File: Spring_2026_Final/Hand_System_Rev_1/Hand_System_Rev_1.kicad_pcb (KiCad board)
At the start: 4 copper layers, 41 parts, among them J1 Barrel_Jack, M1 Motor_Servo, M10 Motor_Servo, M11 Motor_Servo, M2 Motor_Servo, M3 Motor_Servo, M4 Motor_Servo, M5 Motor_Servo, M6 Motor_Servo, M7 Stepper_Motor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

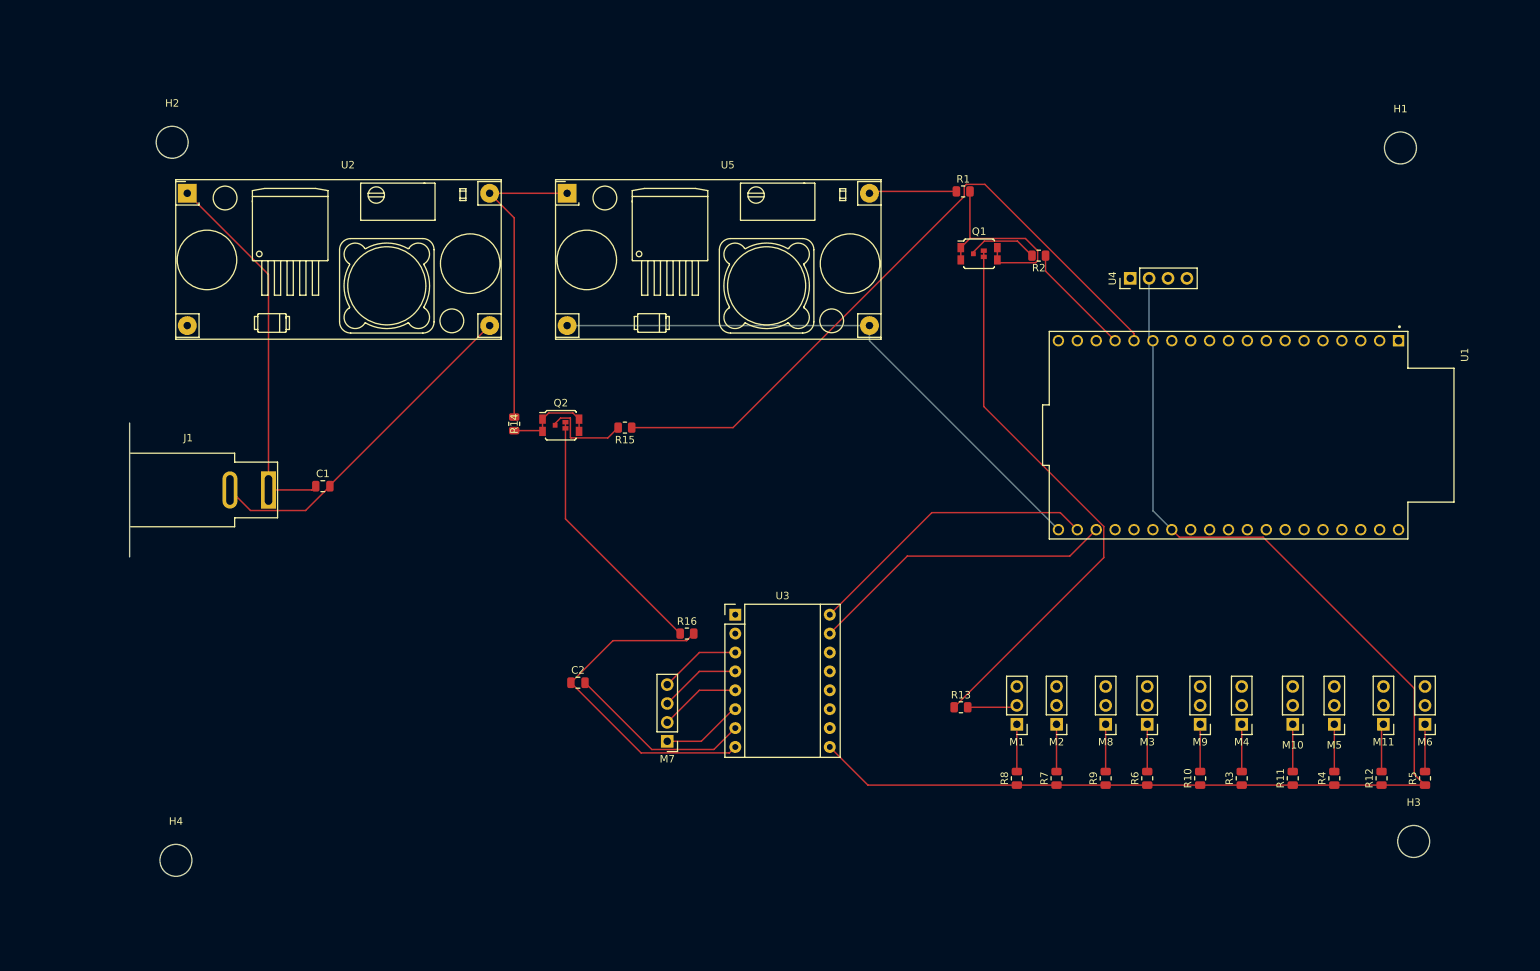
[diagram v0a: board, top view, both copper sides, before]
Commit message: Made PCB with fixed buck coverter 12V to 5v.
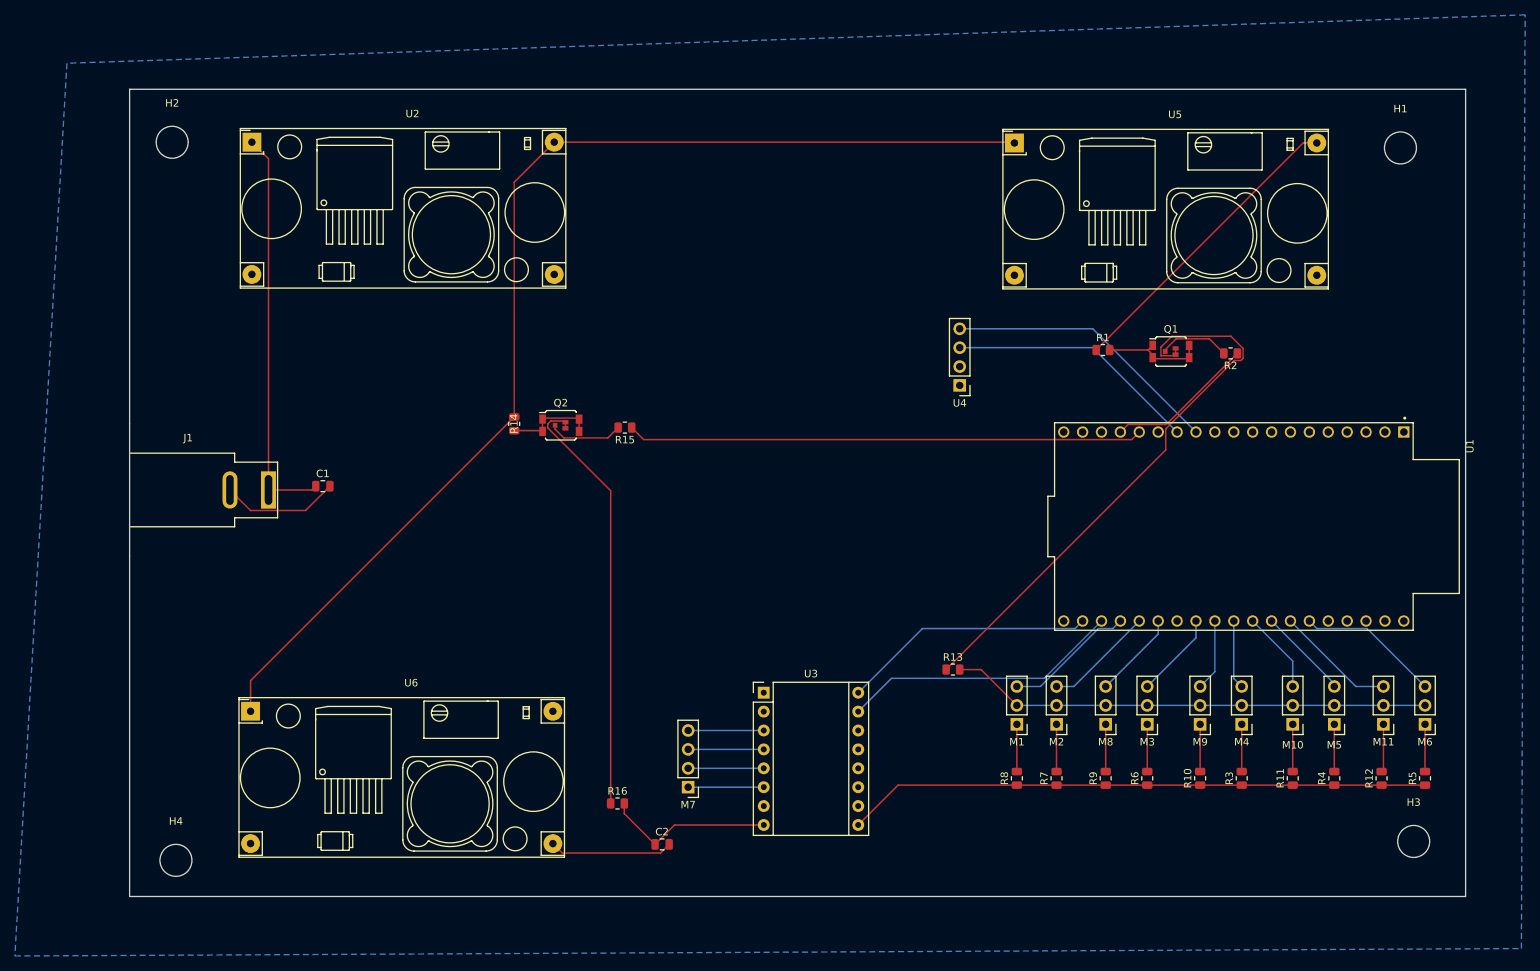
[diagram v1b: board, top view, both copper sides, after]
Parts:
- added U6: LM2596, PCB_Components:LM2596, F.Cu at (75.2, 116.1)
- moved U5 60.5 mm to (177.9, 39.7)
- moved R2 28.9 mm to (206.9, 68.0)
- moved Q1 28.9 mm to (198.9, 67.7)
- moved R1 28.4 mm to (189.7, 67.5)
- moved U4 27.1 mm to (170.5, 72.3), turned to 180 degrees
- moved R16 24.7 mm to (124.5, 128.5)
- moved C2 24.5 mm to (130.5, 134.0)
- moved U1 12.3 mm to (207.3, 91.3)
- moved U3 11.2 mm to (144.2, 113.6)
- moved U2 11.1 mm to (75.4, 39.6)
- moved M7 6.78 mm to (134.0, 126.3)
- moved R13 5.18 mm to (169.6, 110.5)
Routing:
- net 12V: track 41.9 -> 155.3 mm
- net GND: track 386.5 -> 498.0 mm
- net 7.2V: track 11.8 -> 41.2 mm
- net /DT: track 8.59 -> 37.5 mm
- net /CW: track 8.59 -> 33.9 mm
- net Net-(Q2-S): track 34.8 -> 58.0 mm
- net STP_P: track 45.6 -> 22.9 mm
- net /STP_VG: track 91.1 -> 69.3 mm
- net Net-(Q1-D): track 28.2 -> 14.0 mm
- net 5V: track 86.0 -> 99.7 mm
- net /MIDDLE_2: track 21.8 -> 9.25 mm
- net /RING_2: track 24.9 -> 12.3 mm
- net /RING_1: track 23.6 -> 11.0 mm
- net /INDEX_2: track 23.5 -> 11.5 mm
- net /INDEX_1: track 23.7 -> 11.7 mm
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- added copper zone on B.Cu, net GND
- added copper zone on In1.Cu, net GND
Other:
- board outline added: 179.6 x 108.5 mm
